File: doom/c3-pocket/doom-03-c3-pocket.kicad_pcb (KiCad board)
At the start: 2 copper layers, 52 x 128 mm, 58 parts, among them Q1 AO3401A, Q2 FS8205A, SW1 TS-1187A-B-A-B, SW10 PTS645SM43SMTR92 LFS, SW2 TS-1187A-B-A-B, SW3 TS-1187A-B-A-B, SW4 TS-1187A-B-A-B, SW5 TS-1187A-B-A-B, SW6 TS-1187A-B-A-B, SW7 TS-1187A-B-A-B, SW8 TS-1187A-B-A-B, SW9 MSK12C02, U1 ESP32-C3-MINI-1-H4, U2 BQ24075RGTR, U3 DW01A, U4 AP2112K-3.3TRG1, U5 ESD 2-line

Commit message: doom, examples: re-route around the USB-C receptacle's new land pattern
The standard receptacle became GCT USB4105's recommended layout (pcbkit 7e43c086): its shield
legs moved and two unplated guide holes appeared, under the copper these boards had been routed
with (solder-mask-bridge and clearance errors at J1). `build.run` re-routed the 3–5 nets that
crossed it: all seven check complete with 0 errors again; the six Doom boards export for the fab
without --force.

Claude-Session: https://claude.ai/code/session_01GffCzZXi9ShujPbky1eccg
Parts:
- F1: value PTC 680mA -> PTC 500mA
- J1: value (none) -> USB4105-GF-A
- U5: value ESD 2-line -> USBLC6-2SC6
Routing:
- net GND: track 32.6 -> 0.00 mm, vias 31 -> 8

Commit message: Boards pass check and KiCad 10's DRC again: holes in courtyards, the USB net rename
pcbkit's check now has KiCad 10's pth/npth_inside_courtyard (pcbkit be5b6955), and 13 boards
failed it. KiCad's own DRC (kicad-cli 10) reports the same holes on every one of them.

- Parts that really stand above the holes under them (a screen or a Nano on its sockets, the
  Delta-S02's КМ-6 capacitors flat under its chips, as the factory placed them): a courtyard rule
  for the pair, written to each board's .kicad_dru, so KiCad's DRC agrees.
- Real collisions moved: servo-controller's dial 3 mm up (the Nano's socket pins came out under
  it), c3-pocket's fourth M3 hole from under a cell holder to the top edge's middle, s3-rgb's
  D-pad 2 mm up (a holder's peg came through under the down key).
- v003-emu, c3-pocket, rp2040-tft, rp2350-psram, s3-rgb, teensy41: re-routed for the standard USB
  block's renamed net (usb/raw is usb/vbusIn since pcbkit 2088839e): their tracks still carried
  the old name and shorted the fuse and connector pads.
- p4-touch-7: its board file still had a courtyard for the panel the design gives none (KiCad
  reported 114 courtyard errors); written again.

Measured on the dev host: all 44 registry boards `pcbkit check` complete with 0 errors, and
kicad-cli pcb drc 0 errors on every board.

Claude-Session: https://claude.ai/code/session_018URVYF1YPgyrMNetY9yT1T
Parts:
- H1, H2, H3, H4: value (none) -> MountingHole_3.2mm_M3
- logo: value (none) -> Logo_PCBKit_pcbkit.io
- tpBat, tpGnd, tpSys, tpV3: value (none) -> TestPoint_Round_D1.5mm
- moved H4 65.8 mm to (126.0, 76.0)
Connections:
- net usb/power/raw renamed usb/power/vbusIn
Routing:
- net BAT: track 115.3 -> 103.8 mm
- net usb/power/vbusIn: track 15.9 -> 20.4 mm
- net CHG_LED: track 4.32 -> 2.92 mm
- net Net-(C6-1): track 3.86 -> 3.21 mm
- net EN: track 20.7 -> 20.1 mm
- net LCD_DC: track 15.1 -> 14.6 mm

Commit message: doom: a resettable fuse per 18650 cell, a 2 % backlight clamp, a 1 A LDO on the S3 boards
The verifier (wiring-parallel-cells) found the two holders of every Doom board directly in parallel:
a cell put in backwards, or one much fuller than the other, drives the other through nothing but
the cells' resistance (about 56-168 A). Each holder's + now reaches BAT_IN through its own 2 A
resettable fuse (Littelfuse 1812L200/16GR, C18198340: 16 V, 100 A interrupting) on new nets
CELL1_P / CELL2_P. Nothing else moved; the boards were re-routed for the new nets.

- s3-rgb: the MT3608 backlight's open-panel clamp was a 28 V 5 % zener (bound 30.0 V against the
  switch's 30 V). It is now two 2 % zeners in series, UDZVTE-1718B + UDZVTE-1710B (27.33-28.56 V;
  LCSC stocks no single 28 V 2 % part). That is under 29.2 V and above the panel's 27.2 V.
- s3-rgb, s3-handheld: TLV75533 (500 mA) -> TLV75733 (1 A, C485517, same DBV pins; sheet from
  SBVS322C), for the ESP32-S3's 500 mA supply peaks (erc-supply-peak).
- c3-pocket, v003-emu: the USB PTC's hold is 750 mA, as the part (nSMD075) is (rating-current).
- pico2-carrier: the CHG/PG LEDs 1.5 mm further from the display's courtyard. rp2350-handheld:
  the logo off the LCD's courtyard and BT1's peg.
- READMEs: the per-cell fuses, the boards already ordered (s3-rgb, JLC W2026102705013253: insert
  the cells one at a time), status and BOM as check and the fab export give them now.

Measured on the dev host (pcbkit 5e0d2cc8): all 11 complete, 0 errors, 0 unrouted. What is left is
erc-rail-name (sent to the verifier as false positives) and full-speed USB pair coupling. The MCU
pins' nets are unchanged on every board, so the firmware and its simulation are unchanged.

Claude-Session: https://claude.ai/code/session_01B3VRfBCg9vAvGVWujVGarr
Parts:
- added F2: PTC 2000mA, Fuse_1812_4532Metric, B.Cu at (111.8, 101.2)
- added F3: PTC 2000mA, Fuse_1812_4532Metric, B.Cu at (131.8, 99.8)
- F1: value PTC 500mA -> PTC 750mA
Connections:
- BT1 pad 2: BAT_IN -> CELL1_P
- BT2 pad 2: BAT_IN -> CELL2_P
- SW1 pad 2: UP -> GND
- SW10 pad 2: EN -> GND
- SW2 pad 2: DOWN -> GND
- SW3 pad 2: LEFT -> GND
- SW4 pad 2: RIGHT -> GND
- SW5 pad 2: FIRE -> GND
- SW6 pad 2: USE -> GND
- SW7 pad 2: STRAFE -> GND
- SW8 pad 2: MENU -> GND
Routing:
- net CELL2_P: track 0.00 -> 11.2 mm
- net CELL1_P: track 0.00 -> 7.61 mm
- net BAT_IN: track 51.9 -> 58.7 mm, vias 3 -> 1

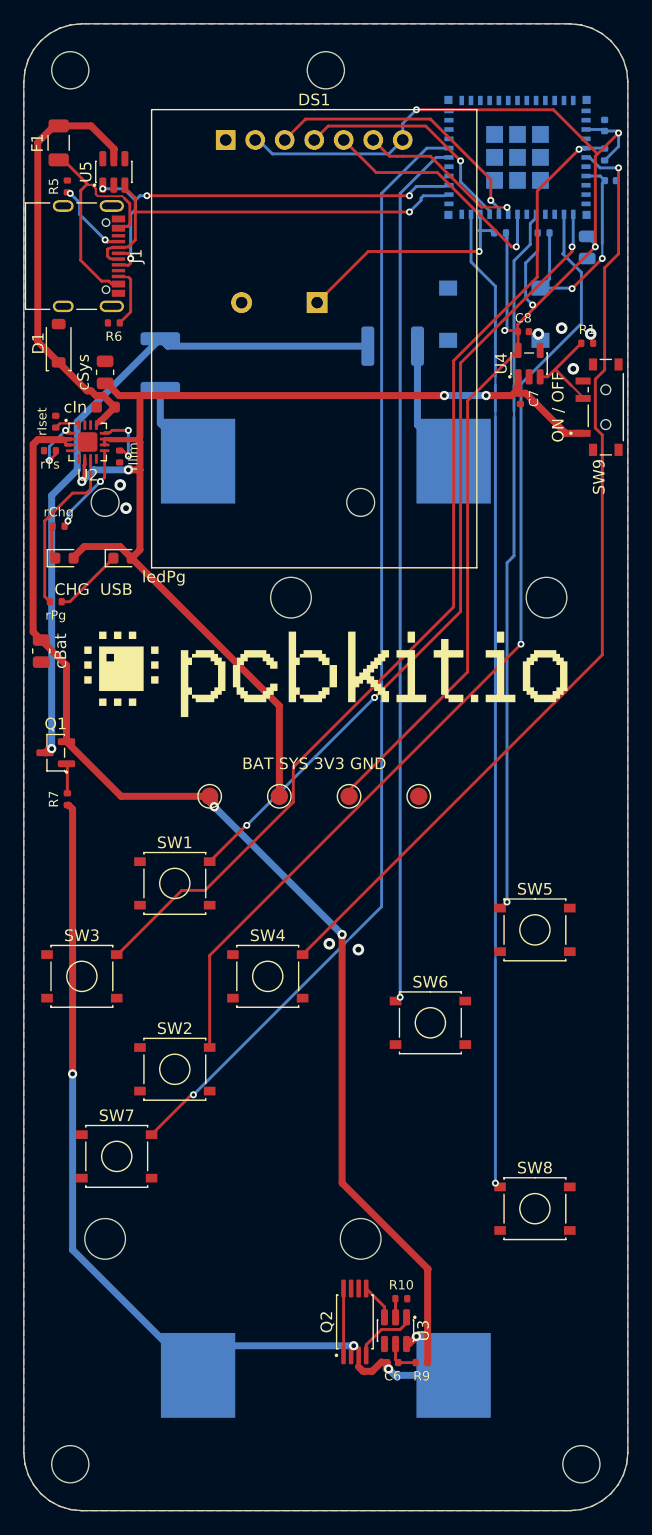
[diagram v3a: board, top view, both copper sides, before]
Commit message: boards: 15 boards rebuilt on pcbkit 20ffacdc9 (their pours under the 0.25 mm hole clearance)
Every board checked with main: 17 of 44 failed on hole-clearance (pours filled before fill c6 made
0.25 mm KiCad's hole clearance the default), keepout (holes now sized by the board) or
place-corner. design.run {} on each (placement and routing kept, pours refilled): 15 now complete,
0 errors. Not here: esp32-p4-touch-lcd-7b and p4-touch-7 (a build reroutes their pairs: 21 and 7
unrouted; kept as they were, 2,372 and 919 hole-clearance errors: a refill without a reroute is
needed).

Claude-Session: https://claude.ai/code/session_01BAgp959tApA8aEg85EYgfb
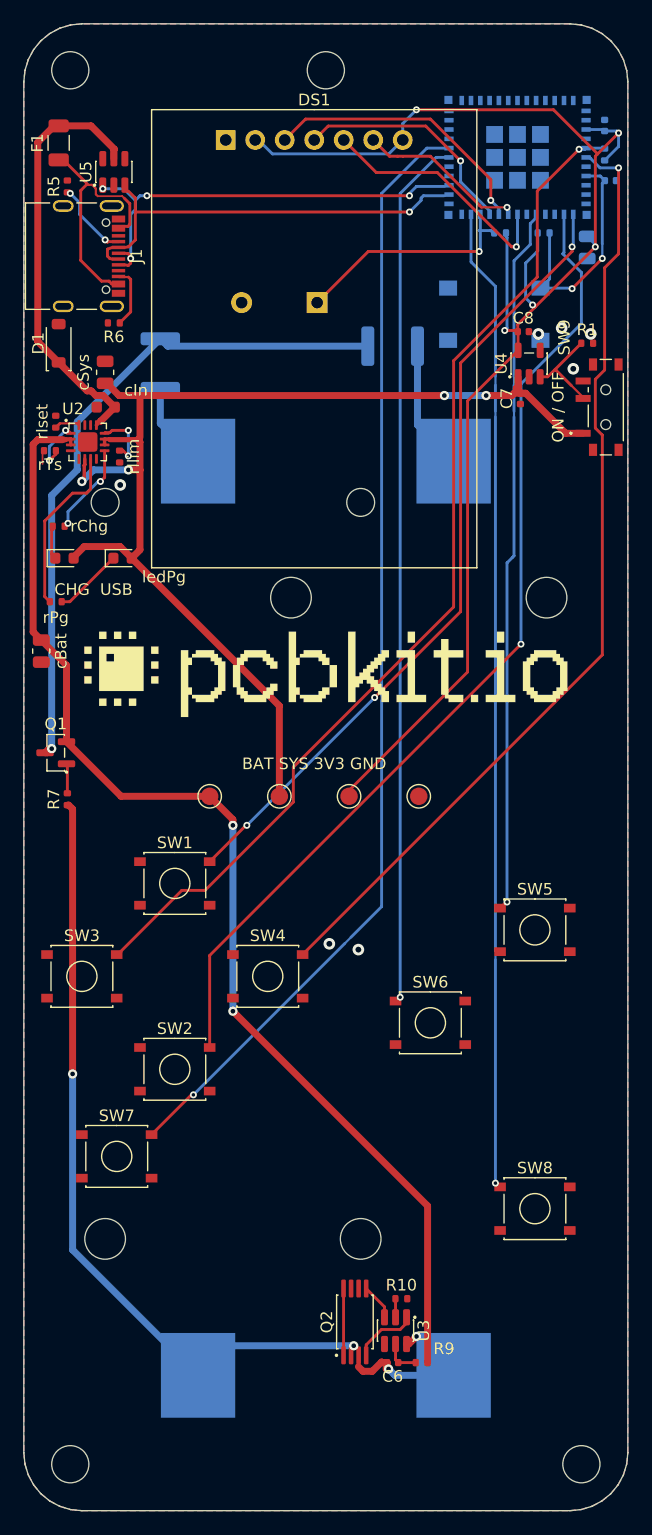
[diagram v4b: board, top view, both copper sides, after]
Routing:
- net BAT: track 103.8 -> 102.0 mm
- net GND: track 0.00 -> 1.20 mm, vias 8 -> 7
